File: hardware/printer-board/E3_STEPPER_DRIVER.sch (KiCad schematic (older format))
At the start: 7 parts, among them J21 MS_SELECT, J22 TO_MOTOR, U12 A4988_MODULE

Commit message: update,
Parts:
- J21: footprint (none) -> Connector_PinHeader_2.54mm:PinHeader_2x03_P2.54mm_Vertical
- J22: footprint (none) -> Connector_PinHeader_2.54mm:PinHeader_1x04_P2.54mm_Vertical
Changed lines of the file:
@@
 EESchema Schematic File Version 4
-LIBS:printer-board-cache
 EELAYER 26 0
 EELAYER END
 $Descr A4 11693 8268
 encoding utf-8
-Sheet 13 27
+Sheet 1 1
 Title ""
 Date ""
@@
 AR Path="/5CC0A8CF/5CC02B38" Ref="U?"  Part="1"
 AR Path="/5CC0AED8/5CC02B38" Ref="U12"  Part="1"
+AR Path="/5CC02B38" Ref="U12"  Part="1"
 F 0 "U12" H 5650 3765 50  0000 C CNN
 F 1 "A4988_MODULE" H 5650 3674 50  0000 C CNN
@@
 AR Path="/5CC0A8CF/5CC04CCD" Ref="R?"  Part="1"
 AR Path="/5CC0AED8/5CC04CCD" Ref="R23"  Part="1"
+AR Path="/5CC04CCD" Ref="R23"  Part="1"
 F 0 "R23" H 4709 2246 50  0000 L CNN
 F 1 "R103,0603" H 4709 2155 50  0000 L CNN
@@
 AR Path="/5CC0A8CF/5CC04CD6" Ref="R?"  Part="1"
 AR Path="/5CC0AED8/5CC04CD6" Ref="R22"  Part="1"
+AR Path="/5CC04CD6" Ref="R22"  Part="1"
 F 0 "R22" H 4292 2746 50  0000 R CNN
 F 1 "R104,0603" H 4292 2655 50  0000 R CNN
@@
 AR Path="/5CC0A8CF/5CC04CDB" Ref="J?"  Part="1"
 AR Path="/5CC0AED8/5CC04CDB" Ref="J21"  Part="1"
+AR Path="/5CC04CDB" Ref="J21"  Part="1"
 F 0 "J21" H 4050 2767 50  0000 C CNN
 F 1 "MS_SELECT" H 4050 2676 50  0000 C CNN
-F 2 "" H 4000 3000 50  0001 C CNN
+F 2 "Connector_PinHeader_2.54mm:PinHeader_2x03_P2.54mm_Vertical" H 4000 3000 50  0001 C CNN
 F 3 "~" H 4000 3000 50  0001 C CNN
 	1    4000 3000
@@
 AR Path="/5CC0A8CF/5CC04CE4" Ref="#PWR?"  Part="1"
 AR Path="/5CC0AED8/5CC04CE4" Ref="#PWR0214"  Part="1"
+AR Path="/5CC04CE4" Ref="#PWR0214"  Part="1"
 F 0 "#PWR0214" H 4350 2250 50  0001 C CNN
 F 1 "GND" H 4355 2327 50  0000 C CNN
@@
 AR Path="/5CC0A8CF/5CC04CF0" Ref="#PWR?"  Part="1"
 AR Path="/5CC0AED8/5CC04CF0" Ref="#PWR0215"  Part="1"
+AR Path="/5CC04CF0" Ref="#PWR0215"  Part="1"
 F 0 "#PWR0215" H 6600 2400 50  0001 C CNN
 F 1 "+12V" H 6615 2723 50  0000 C CNN
@@
 AR Path="/5CC0A8CF/5CC04CFA" Ref="#PWR?"  Part="1"
 AR Path="/5CC0AED8/5CC04CFA" Ref="#PWR0216"  Part="1"
+AR Path="/5CC04CFA" Ref="#PWR0216"  Part="1"
 F 0 "#PWR0216" H 6600 2650 50  0001 C CNN
 F 1 "GND" V 6605 2772 50  0000 R CNN
@@
 AR Path="/5CC0A8CF/5CC04CFF" Ref="J?"  Part="1"
 AR Path="/5CC0AED8/5CC04CFF" Ref="J22"  Part="1"
+AR Path="/5CC04CFF" Ref="J22"  Part="1"
 F 0 "J22" H 6980 3092 50  0000 L CNN
 F 1 "TO_MOTOR" H 6980 3001 50  0000 L CNN
-F 2 "" H 6900 3100 50  0001 C CNN
+F 2 "Connector_PinHeader_2.54mm:PinHeader_1x04_P2.54mm_Vertical" H 6900 3100 50  0001 C CNN
 F 3 "~" H 6900 3100 50  0001 C CNN
 	1    6900 3100
@@
 AR Path="/5CC0A8CF/5CC04263" Ref="#PWR?"  Part="1"
 AR Path="/5CC0AED8/5CC04263" Ref="#PWR0217"  Part="1"
+AR Path="/5CC04263" Ref="#PWR0217"  Part="1"
 F 0 "#PWR0217" H 6600 3250 50  0001 C CNN
 F 1 "GND" V 6477 3463 50  0000 C CNN
@@
 AR Path="/5CC0A8CF/5CC04D14" Ref="#PWR?"  Part="1"
 AR Path="/5CC0AED8/5CC04D14" Ref="#PWR0218"  Part="1"
+AR Path="/5CC04D14" Ref="#PWR0218"  Part="1"
 F 0 "#PWR0218" H 3500 2550 50  0001 C CNN
 F 1 "+5V" H 3515 2873 50  0000 C CNN
@@
 AR Path="/5CC0A8CF/5CC06096" Ref="#PWR?"  Part="1"
 AR Path="/5CC0AED8/5CC06096" Ref="#PWR0219"  Part="1"
+AR Path="/5CC06096" Ref="#PWR0219"  Part="1"
 F 0 "#PWR0219" H 4650 1800 50  0001 C CNN
 F 1 "+5V" H 4665 2123 50  0000 C CNN
@@
 AR Path="/5CC0A8CF/5CC04D21" Ref="#PWR?"  Part="1"
 AR Path="/5CC0AED8/5CC04D21" Ref="#PWR0220"  Part="1"
+AR Path="/5CC04D21" Ref="#PWR0220"  Part="1"
 F 0 "#PWR0220" H 6600 3250 50  0001 C CNN
 F 1 "+5V" V 6615 3528 50  0000 L CNN
@@
 AR Path="/5CC0A8CF/5CC04D2C" Ref="#PWR?"  Part="1"
 AR Path="/5CC0AED8/5CC04D2C" Ref="#PWR0221"  Part="1"
+AR Path="/5CC04D2C" Ref="#PWR0221"  Part="1"
 F 0 "#PWR0221" H 5400 3900 50  0001 C CNN
 F 1 "+12V" V 5415 4178 50  0000 L CNN
@@
 AR Path="/5CC0A8CF/5CC04D31" Ref="C?"  Part="1"
 AR Path="/5CC0AED8/5CC04D31" Ref="C24"  Part="1"
+AR Path="/5CC04D31" Ref="C24"  Part="1"
 F 0 "C24" V 5875 4050 50  0000 C CNN
 F 1 "CP100uf,25V" V 5784 4050 50  0000 C CNN
@@
 AR Path="/5CC0A8CF/5CC04D40" Ref="#PWR?"  Part="1"
 AR Path="/5CC0AED8/5CC04D40" Ref="#PWR0222"  Part="1"
+AR Path="/5CC04D40" Ref="#PWR0222"  Part="1"
 F 0 "#PWR0222" H 5950 3800 50  0001 C CNN
 F 1 "GND" V 5955 3922 50  0000 R CNN
@@
 AR Path="/5CC0A8CF/5CC04D4A" Ref="C?"  Part="1"
 AR Path="/5CC0AED8/5CC04D4A" Ref="C25"  Part="1"
+AR Path="/5CC04D4A" Ref="C25"  Part="1"
 F 0 "C25" V 5517 4250 50  0000 C CNN
 F 1 "CP100uf,25V" V 5426 4250 50  0000 C CNN
@@
 AR Path="/5CC0A8CF/5CC04D4E" Ref="#PWR?"  Part="1"
 AR Path="/5CC0AED8/5CC04D4E" Ref="#PWR0223"  Part="1"
+AR Path="/5CC04D4E" Ref="#PWR0223"  Part="1"
 F 0 "#PWR0223" H 5950 4000 50  0001 C CNN
 F 1 "GND" V 5955 4122 50  0000 R CNN
@@
 AR Path="/5CC0A8CF/5CC04D57" Ref="#PWR?"  Part="1"
 AR Path="/5CC0AED8/5CC04D57" Ref="#PWR0224"  Part="1"
+AR Path="/5CC04D57" Ref="#PWR0224"  Part="1"
 F 0 "#PWR0224" H 5400 4100 50  0001 C CNN
 F 1 "+5V" V 5415 4378 50  0000 L CNN

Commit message: update,
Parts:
- J22: footprint Connector_PinHeader_2.54mm:PinHeader_1x04_P2.54mm_Vertical -> footprint-lib:s4b-ph-kl,stepper_motor_terminal
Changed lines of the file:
@@
 EESchema Schematic File Version 4
+LIBS:printer-board-cache
 EELAYER 26 0
 EELAYER END
 $Descr A4 11693 8268
 encoding utf-8
-Sheet 1 1
+Sheet 1 35
 Title ""
 Date ""
@@
 F 0 "J22" H 6980 3092 50  0000 L CNN
 F 1 "TO_MOTOR" H 6980 3001 50  0000 L CNN
-F 2 "Connector_PinHeader_2.54mm:PinHeader_1x04_P2.54mm_Vertical" H 6900 3100 50  0001 C CNN
+F 2 "footprint-lib:s4b-ph-kl,stepper_motor_terminal" H 6900 3100 50  0001 C CNN
 F 3 "~" H 6900 3100 50  0001 C CNN
 	1    6900 3100

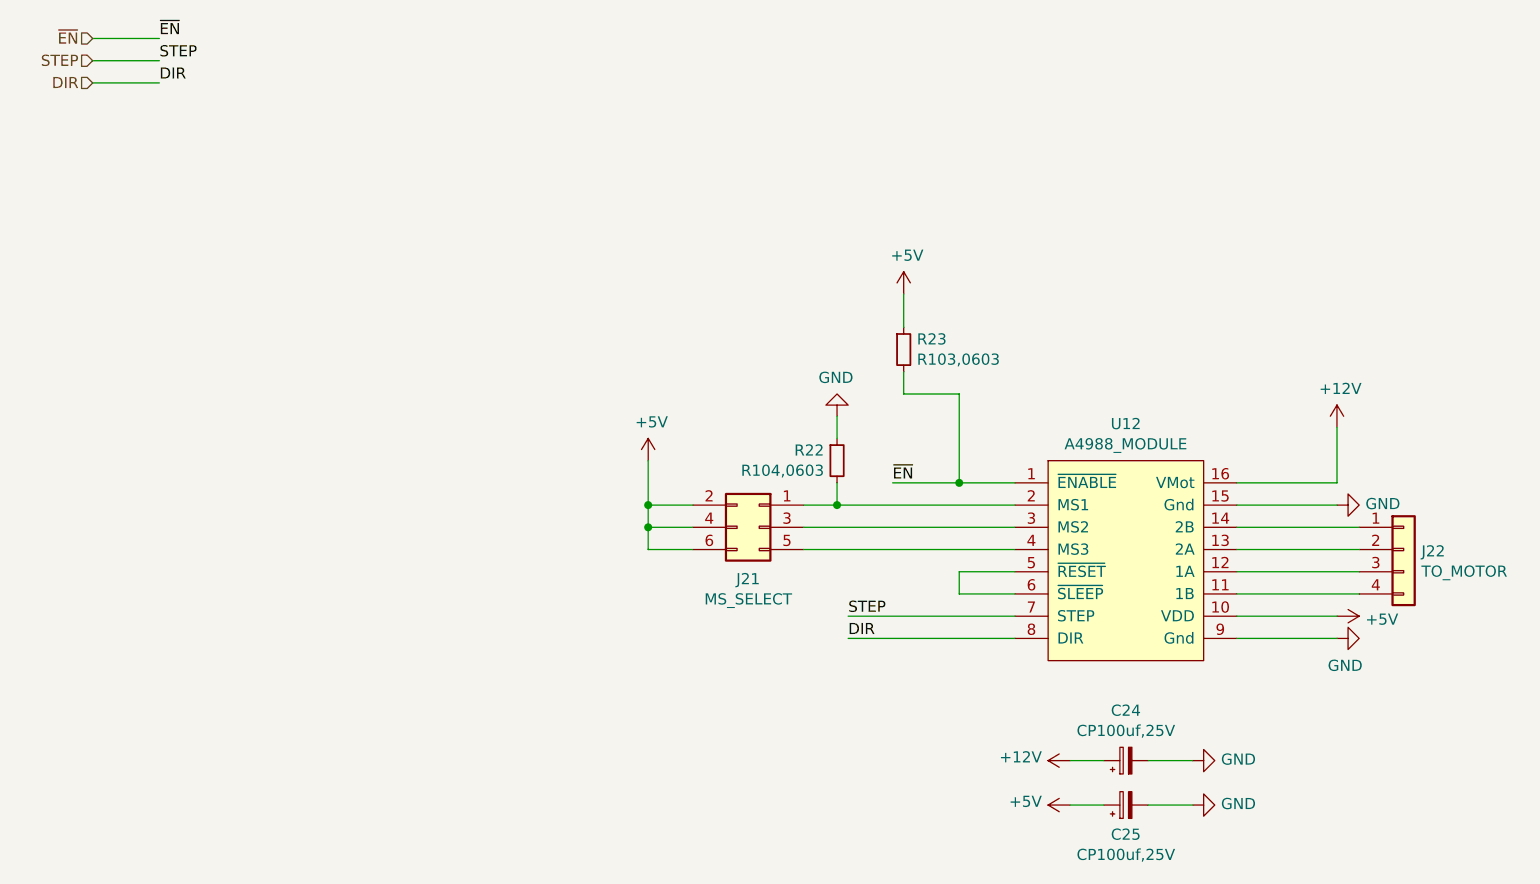
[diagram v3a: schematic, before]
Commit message: update for stepper motor circuit,
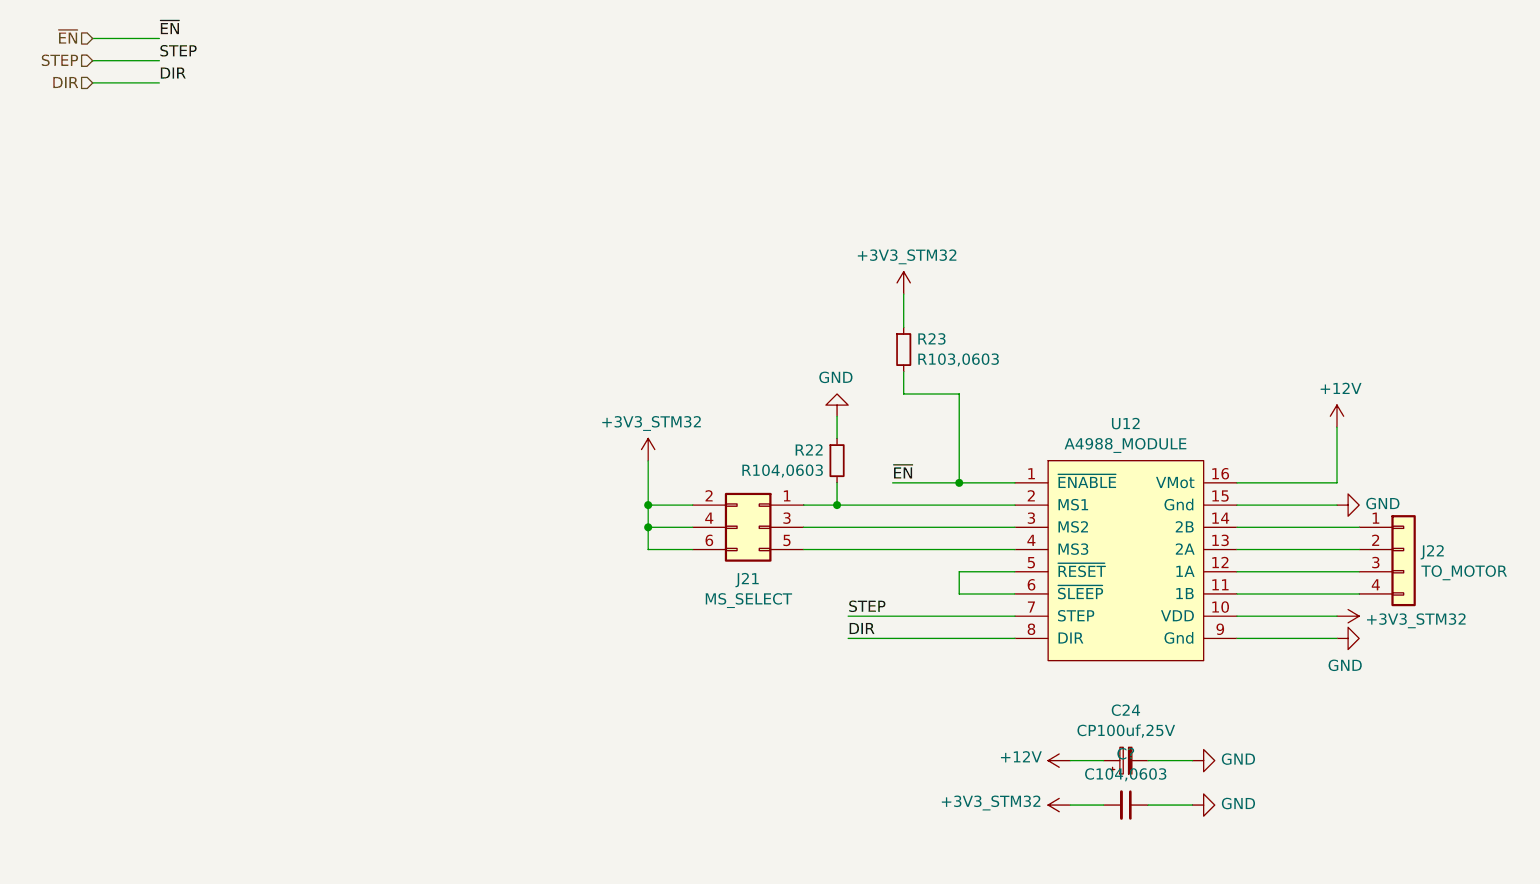
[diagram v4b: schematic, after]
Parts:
- removed C25: CP100uf,25V, Capacitor_SMD:CP_Elec_6.3x7.7, symbol taobao-cp:CP100uf,25V
- added C?: C104,0603, Capacitor_SMD:C_0603_1608Metric_Pad1.05x0.95mm_HandSolder, symbol taobao-c:C104,0603
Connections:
- net GND: now also C?.1
- net +5V renamed +3V3_STM32
- net +3V3_STM32: now also C?.2
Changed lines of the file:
@@
 EESchema Schematic File Version 4
-LIBS:printer-board-cache
+LIBS:E3_STEPPER_DRIVER-cache
 EELAYER 26 0
 EELAYER END
 $Descr A4 11693 8268
 encoding utf-8
-Sheet 1 35
+Sheet 1 1
 Title ""
 Date ""
@@
 	3500 3100 3700 3100
 $Comp
-L power:+5V #PWR?
-U 1 1 5CC04D14
-P 3500 2700
-AR Path="/5CC02AB8/5CC04D14" Ref="#PWR?"  Part="1"
-AR Path="/5CC0A4B9/5CC04D14" Ref="#PWR?"  Part="1"
-AR Path="/5CC0A53C/5CC04D14" Ref="#PWR?"  Part="1"
-AR Path="/5CC0A8C5/5CC04D14" Ref="#PWR?"  Part="1"
-AR Path="/5CC0A8CA/5CC04D14" Ref="#PWR?"  Part="1"
-AR Path="/5CC0A8CF/5CC04D14" Ref="#PWR?"  Part="1"
-AR Path="/5CC0AED8/5CC04D14" Ref="#PWR0218"  Part="1"
-AR Path="/5CC04D14" Ref="#PWR0218"  Part="1"
-F 0 "#PWR0218" H 3500 2550 50  0001 C CNN
-F 1 "+5V" H 3515 2873 50  0000 C CNN
-F 2 "" H 3500 2700 50  0001 C CNN
-F 3 "" H 3500 2700 50  0001 C CNN
-	1    3500 2700
-	1    0    0    -1
-$EndComp
-$Comp
-L power:+5V #PWR?
-U 1 1 5CC06096
-P 4650 1950
-AR Path="/5CC02AB8/5CC06096" Ref="#PWR?"  Part="1"
-AR Path="/5CC0A4B9/5CC06096" Ref="#PWR?"  Part="1"
-AR Path="/5CC0A53C/5CC06096" Ref="#PWR?"  Part="1"
-AR Path="/5CC0A8C5/5CC06096" Ref="#PWR?"  Part="1"
-AR Path="/5CC0A8CA/5CC06096" Ref="#PWR?"  Part="1"
-AR Path="/5CC0A8CF/5CC06096" Ref="#PWR?"  Part="1"
-AR Path="/5CC0AED8/5CC06096" Ref="#PWR0219"  Part="1"
-AR Path="/5CC06096" Ref="#PWR0219"  Part="1"
-F 0 "#PWR0219" H 4650 1800 50  0001 C CNN
-F 1 "+5V" H 4665 2123 50  0000 C CNN
-F 2 "" H 4650 1950 50  0001 C CNN
-F 3 "" H 4650 1950 50  0001 C CNN
-	1    4650 1950
-	1    0    0    -1
-$EndComp
-$Comp
-L power:+5V #PWR?
-U 1 1 5CC04D21
-P 6600 3400
-AR Path="/5CC02AB8/5CC04D21" Ref="#PWR?"  Part="1"
-AR Path="/5CC0A4B9/5CC04D21" Ref="#PWR?"  Part="1"
-AR Path="/5CC0A53C/5CC04D21" Ref="#PWR?"  Part="1"
-AR Path="/5CC0A8C5/5CC04D21" Ref="#PWR?"  Part="1"
-AR Path="/5CC0A8CA/5CC04D21" Ref="#PWR?"  Part="1"
-AR Path="/5CC0A8CF/5CC04D21" Ref="#PWR?"  Part="1"
-AR Path="/5CC0AED8/5CC04D21" Ref="#PWR0220"  Part="1"
-AR Path="/5CC04D21" Ref="#PWR0220"  Part="1"
-F 0 "#PWR0220" H 6600 3250 50  0001 C CNN
-F 1 "+5V" V 6615 3528 50  0000 L CNN
-F 2 "" H 6600 3400 50  0001 C CNN
-F 3 "" H 6600 3400 50  0001 C CNN
-	1    6600 3400
-	0    1    1    0
-$EndComp
-$Comp
 L power:+12V #PWR?
 U 1 1 5CC04D2C
@@
 	3500 3000 3500 3100
 $Comp
-L taobao-cp:CP100uf,25V C?
-U 1 1 5CC04D4A
-P 5650 4250
-AR Path="/5CC02AB8/5CC04D4A" Ref="C?"  Part="1"
-AR Path="/5CC0A4B9/5CC04D4A" Ref="C?"  Part="1"
-AR Path="/5CC0A53C/5CC04D4A" Ref="C?"  Part="1"
-AR Path="/5CC0A8C5/5CC04D4A" Ref="C?"  Part="1"
-AR Path="/5CC0A8CA/5CC04D4A" Ref="C?"  Part="1"
-AR Path="/5CC0A8CF/5CC04D4A" Ref="C?"  Part="1"
-AR Path="/5CC0AED8/5CC04D4A" Ref="C25"  Part="1"
-AR Path="/5CC04D4A" Ref="C25"  Part="1"
-F 0 "C25" V 5517 4250 50  0000 C CNN
-F 1 "CP100uf,25V" V 5426 4250 50  0000 C CNN
-F 2 "Capacitor_SMD:CP_Elec_6.3x7.7" H 5650 4250 50  0001 C CNN
-F 3 "~" H 5650 4250 50  0001 C CNN
-	1    5650 4250
-	0    -1   -1   0
-$EndComp
-$Comp
 L power:GND #PWR?
 U 1 1 5CC04D4E
@@
 Wire Wire Line
 	5750 4250 5950 4250
-$Comp
-L power:+5V #PWR?
-U 1 1 5CC04D57
-P 5400 4250
-AR Path="/5CC02AB8/5CC04D57" Ref="#PWR?"  Part="1"
-AR Path="/5CC0A4B9/5CC04D57" Ref="#PWR?"  Part="1"
-AR Path="/5CC0A53C/5CC04D57" Ref="#PWR?"  Part="1"
-AR Path="/5CC0A8C5/5CC04D57" Ref="#PWR?"  Part="1"
-AR Path="/5CC0A8CA/5CC04D57" Ref="#PWR?"  Part="1"
-AR Path="/5CC0A8CF/5CC04D57" Ref="#PWR?"  Part="1"
-AR Path="/5CC0AED8/5CC04D57" Ref="#PWR0224"  Part="1"
-AR Path="/5CC04D57" Ref="#PWR0224"  Part="1"
-F 0 "#PWR0224" H 5400 4100 50  0001 C CNN
-F 1 "+5V" V 5415 4378 50  0000 L CNN
-F 2 "" H 5400 4250 50  0001 C CNN
-F 3 "" H 5400 4250 50  0001 C CNN
-	1    5400 4250
-	0    -1   -1   0
-$EndComp
 Text HLabel 1000 800  0    50   Input ~ 0
 ~EN~
@@
 EndData
 $EndBitmap
+$Comp
+L taobao-components:+3V3_STM32 #PWR?
+U 1 1 5CC40A01
+P 4650 1950
+F 0 "#PWR?" H 4650 1800 50  0001 C CNN
+F 1 "+3V3_STM32" H 4665 2123 50  0000 C CNN
+F 2 "" H 4650 1950 50  0001 C CNN
+F 3 "" H 4650 1950 50  0001 C CNN
+	1    4650 1950
+	1    0    0    -1
+$EndComp
+$Comp
+L taobao-components:+3V3_STM32 #PWR?
+U 1 1 5CC40AC0
+P 3500 2700
+F 0 "#PWR?" H 3500 2550 50  0001 C CNN
+F 1 "+3V3_STM32" H 3515 2873 50  0000 C CNN
+F 2 "" H 3500 2700 50  0001 C CNN
+F 3 "" H 3500 2700 50  0001 C CNN
+	1    3500 2700
+	1    0    0    -1
+$EndComp
+$Comp
+L taobao-components:+3V3_STM32 #PWR?
+U 1 1 5CC40B4A
+P 5400 4250
+F 0 "#PWR?" H 5400 4100 50  0001 C CNN
+F 1 "+3V3_STM32" V 5415 4378 50  0000 L CNN
+F 2 "" H 5400 4250 50  0001 C CNN
+F 3 "" H 5400 4250 50  0001 C CNN
+	1    5400 4250
+	0    -1   -1   0
+$EndComp
+$Comp
+L taobao-components:+3V3_STM32 #PWR?
+U 1 1 5CC40BB8
+P 6600 3400
+F 0 "#PWR?" H 6600 3250 50  0001 C CNN
+F 1 "+3V3_STM32" V 6615 3528 50  0000 L CNN
+F 2 "" H 6600 3400 50  0001 C CNN
+F 3 "" H 6600 3400 50  0001 C CNN
+	1    6600 3400
+	0    1    1    0
+$EndComp
+$Comp
+L taobao-c:C104,0603 C?
+U 1 1 5CC40D3E
+P 5650 4250
+F 0 "C?" V 5421 4250 50  0000 C CNN
+F 1 "C104,0603" V 5512 4250 50  0000 C CNN
+F 2 "Capacitor_SMD:C_0603_1608Metric_Pad1.05x0.95mm_HandSolder" H 5650 4250 50  0001 C CNN
+F 3 "~" H 5650 4250 50  0001 C CNN
+	1    5650 4250
+	0    1    1    0
+$EndComp
 $EndSCHEMATC
